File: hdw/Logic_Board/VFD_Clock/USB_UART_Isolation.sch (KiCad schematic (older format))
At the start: 12 parts

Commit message: Resurrected project
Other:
- moved on the sheet: C?, R?, U?

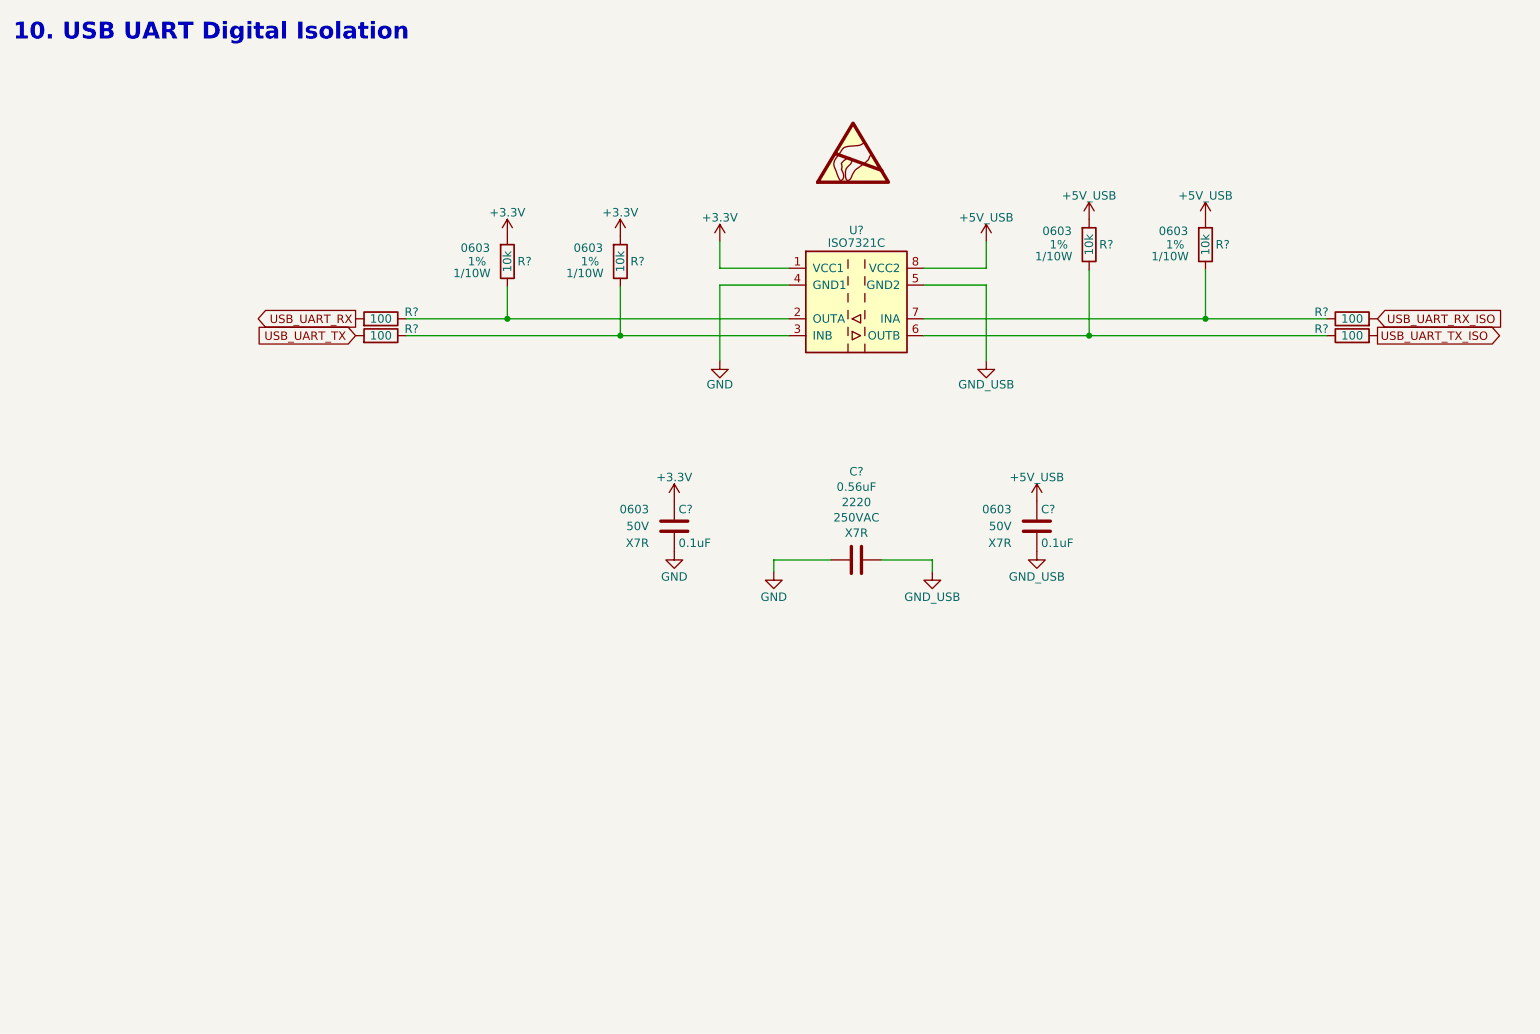
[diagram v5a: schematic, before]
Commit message: Added USB telemetry, isolation, and POS60_VAN current sense
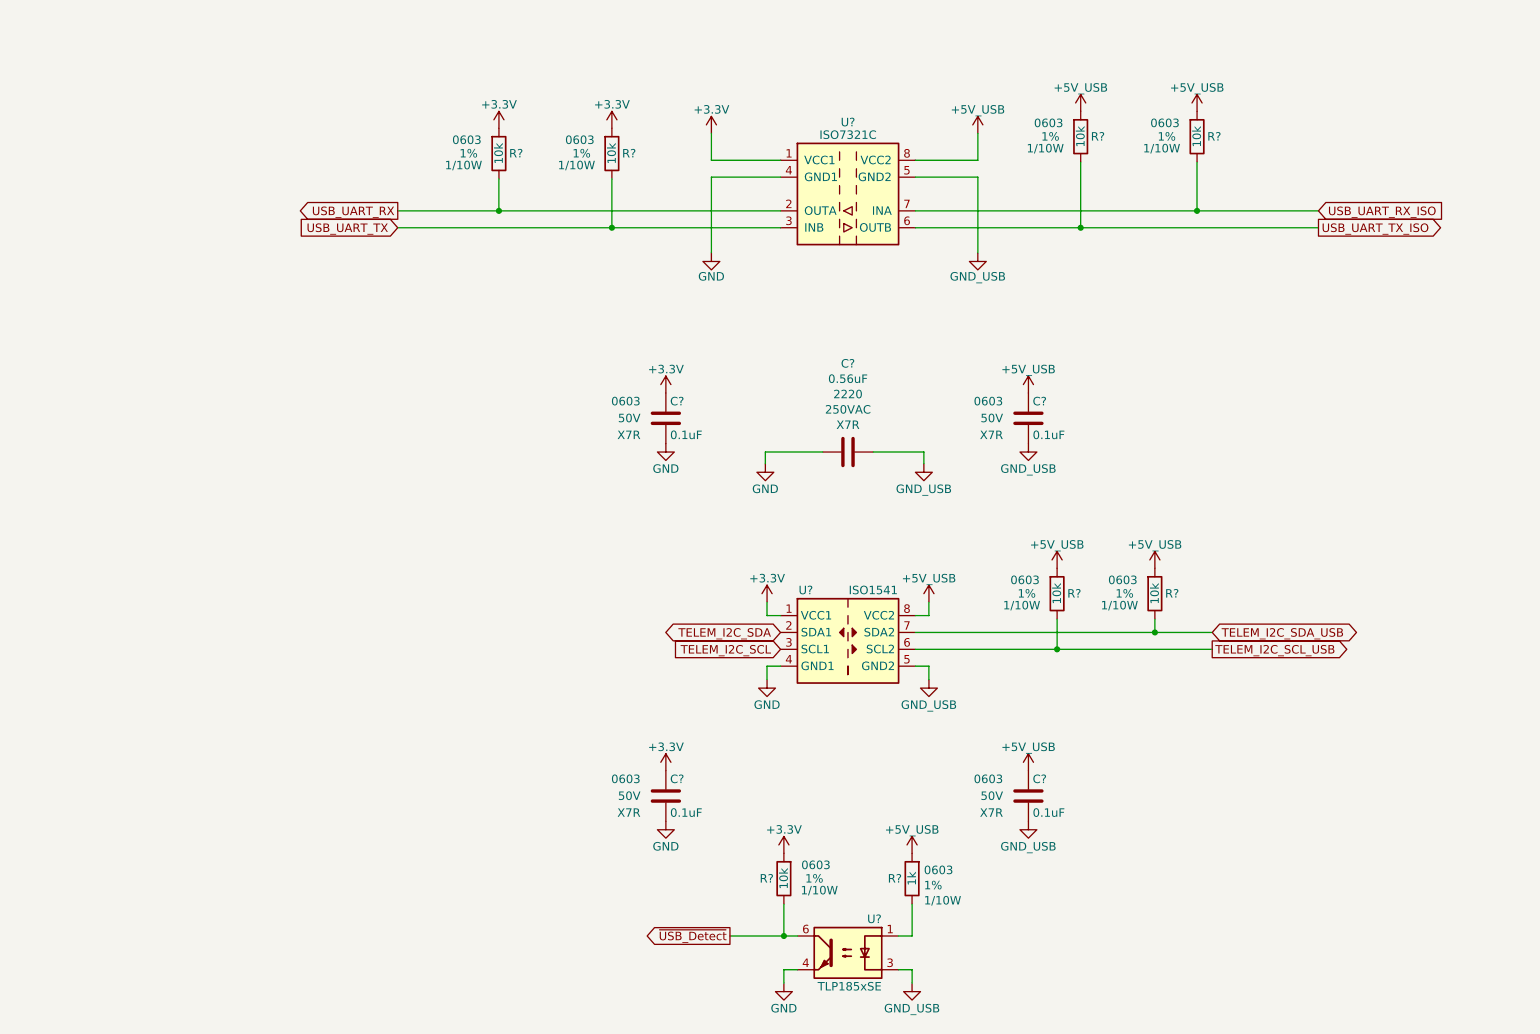
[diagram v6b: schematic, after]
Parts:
- removed R? (x4): 100, Resistors_SMD:R_0603, symbol Custom_Library:R_Custom
- added C? (x2): 0.1uF, Capacitors_SMD:C_0603, symbol Custom_Library:C_Custom
- added R? (x3): 10k, Resistors_SMD:R_0603, symbol Custom_Library:R_Custom
- added R?: 1k, symbol Custom_Library:R_Custom
- added U?: ISO1541, Package_SO:SOIC-8_3.9x4.9mm_P1.27mm, symbol Isolator:ISO1541
- added U?: TLP185xSE, Package_SO:SOIC-4_4.55x3.7mm_P2.54mm, symbol Isolator:TLP185xSE
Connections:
- net +3V3: now also C?.1, R?.1, U?.1 (VCC1)
- net +5V_USB: now also C?.1, R?.1, R?.1, R?.1, U?.8 (VCC2)
- net GND: now also C?.2, U?.4, U?.4 (GND1)
- net GND_USB: now also C?.2, U?.3, U?.5 (GND2)
- net USB_UART_RX: now also R?.2, U?.2 (OUTA)
- net USB_UART_RX_ISO: now also R?.2, U?.7 (INA)
- net USB_UART_TX: now also R?.2, U?.3 (INB)
- net USB_UART_TX_ISO: now also R?.2, U?.6 (OUTB)
- new net: R?.2, U?.1
- new net TELEM_I2C_SCL: U?.3 (SCL1)
- new net TELEM_I2C_SCL_USB: R?.2, U?.6 (SCL2)
- new net TELEM_I2C_SDA: U?.2 (SDA1)
- new net TELEM_I2C_SDA_USB: R?.2, U?.7 (SDA2)
- new net ~USB_Detect: R?.2, U?.6
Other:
- note removed: "10. USB UART Digital Isolation"
- moved on the sheet: C?, R?, U?

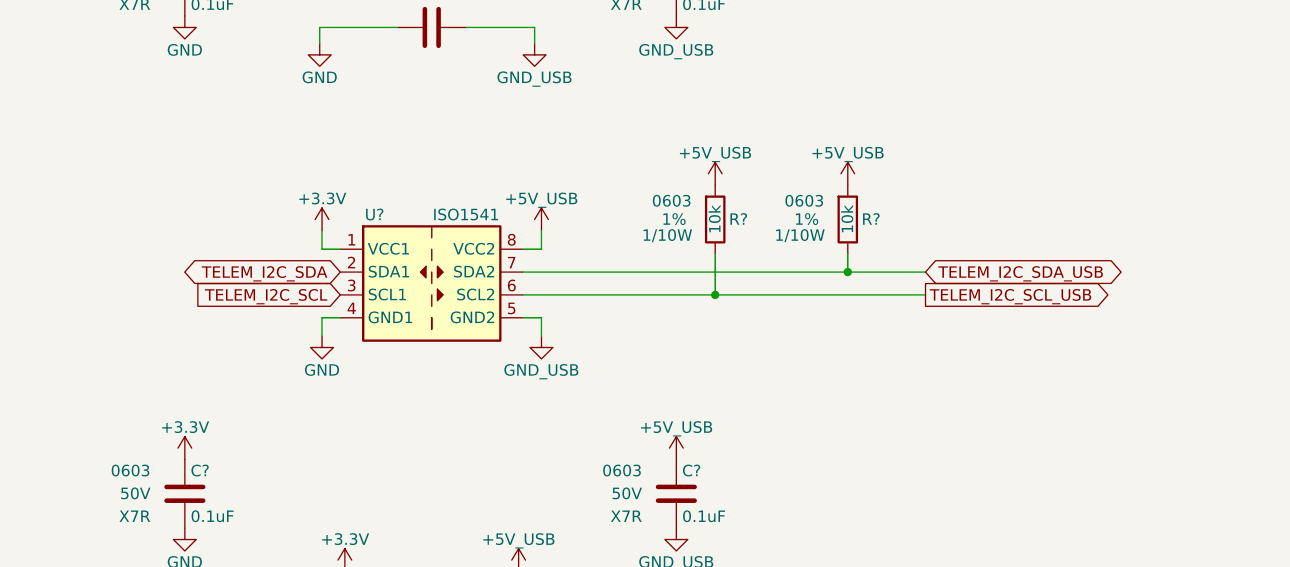
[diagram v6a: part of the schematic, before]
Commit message: Lots of schematic additions
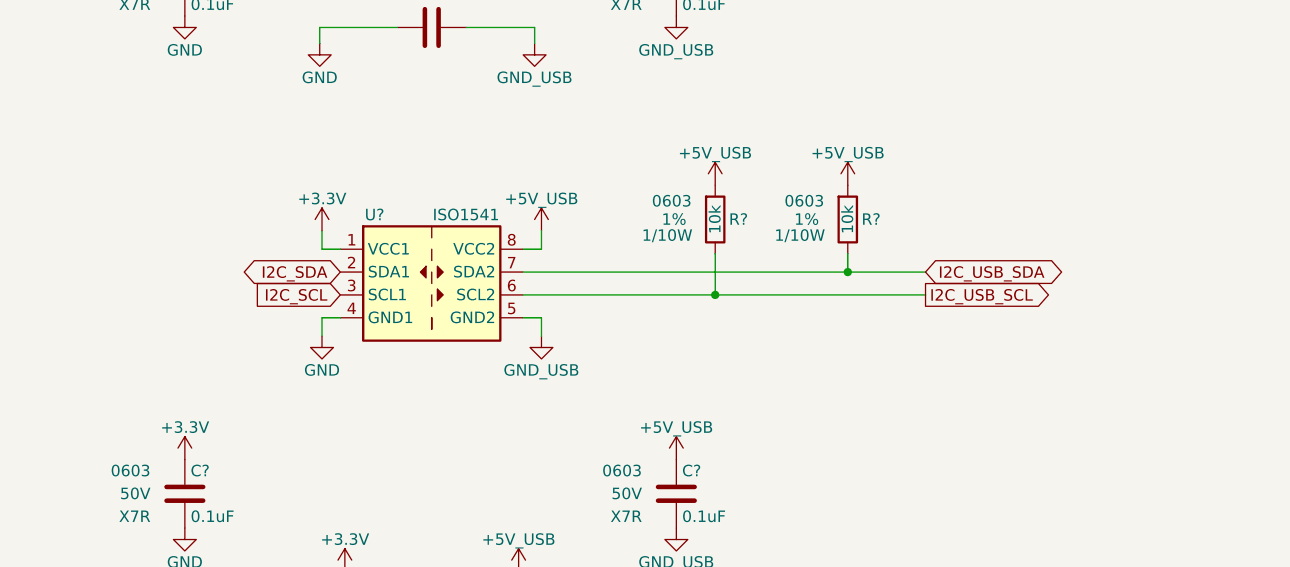
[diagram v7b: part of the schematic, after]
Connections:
- net TELEM_I2C_SCL renamed I2C_SCL
- net TELEM_I2C_SCL_USB renamed I2C_USB_SCL
- net TELEM_I2C_SDA renamed I2C_SDA
- net TELEM_I2C_SDA_USB renamed I2C_USB_SDA
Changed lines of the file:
@@
 $Descr A 11000 8500
 encoding utf-8
-Sheet 7 26
+Sheet 7 28
 Title "VFD Clock"
 Date "2019-04-11"
@@
 $EndComp
 Text GLabel 5100 4200 0    50   BiDi ~ 0
-TELEM_I2C_SDA
+I2C_SDA
 Text GLabel 5100 4300 0    50   Input ~ 0
-TELEM_I2C_SCL
+I2C_SCL
 Wire Wire Line
 	7660 4200 7320 4200
@@
 $EndComp
 Text GLabel 7660 4300 2    50   Output ~ 0
-TELEM_I2C_SCL_USB
+I2C_USB_SCL
 Text GLabel 7660 4200 2    50   BiDi ~ 0
-TELEM_I2C_SDA_USB
+I2C_USB_SDA
 $Comp
 L Custom_Library:C_Custom C?

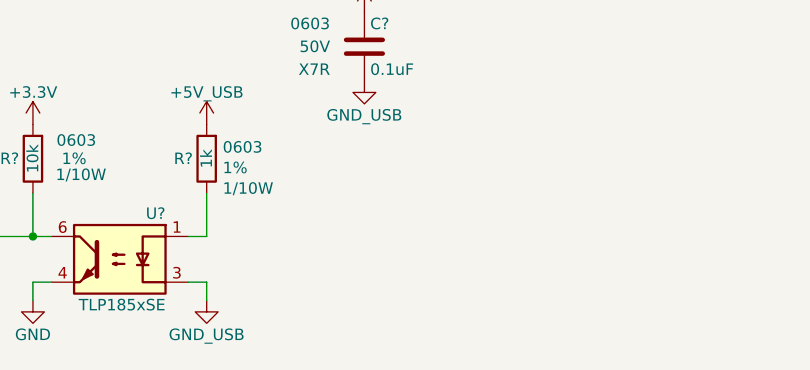
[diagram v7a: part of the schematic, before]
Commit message: Started IV-6 display board, continued logic board development
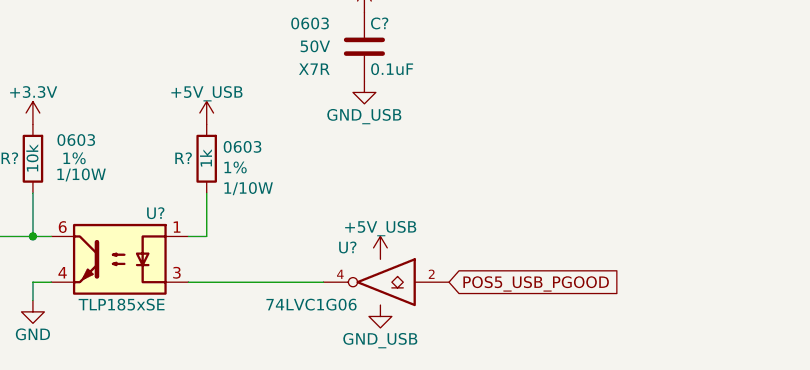
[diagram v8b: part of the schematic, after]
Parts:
- added U?: 74LVC1G06, TO_SOT_Packages_SMD:SOT-353_SC-70-5, symbol Custom_Library:74LVC1G06_Power
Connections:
- net +5V_USB: now also U?.5 (VCC)
- net GND_USB: now also U?.3 (GND); no longer U?.3
- new net: U?.3, U?.4
- new net POS5_USB_PGOOD: U?.2
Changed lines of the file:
@@
 	1    0    0    -1
 $EndComp
-$Comp
-L Custom_Library:GND_USB #PWR?
-U 1 1 5E0AFA5F
-P 5880 6280
-F 0 "#PWR?" H 5880 6030 50  0001 C CNN
-F 1 "GND_USB" H 5880 6130 50  0000 C CNN
-F 2 "" H 5880 6280 50  0001 C CNN
-F 3 "" H 5880 6280 50  0001 C CNN
-	1    5880 6280
-	1    0    0    -1
-$EndComp
-Wire Wire Line
-	5880 6280 5880 6200
-Wire Wire Line
-	5880 6200 5800 6200
 Wire Wire Line
 	5120 6280 5120 6200
@@
 Wire Wire Line
 	5120 6000 5120 5810
+Text GLabel 4800 6000 0    50   Output ~ 0
+~USB_Detect
+Wire Wire Line
+	4800 6000 5120 6000
+Connection ~ 5120 6000
+$Comp
+L Custom_Library:+5V_USB #PWR?
+U 1 1 5E0BA4BC
+P 5880 5510
+AR Path="/5BAAE1F3/5E0BA4BC" Ref="#PWR?"  Part="1"
+AR Path="/5BAAE1DC/5E0BA4BC" Ref="#PWR?"  Part="1"
+AR Path="/5CAD2DA3/5E0BA4BC" Ref="#PWR?"  Part="1"
+F 0 "#PWR?" H 5880 5360 50  0001 C CNN
+F 1 "+5V_USB" H 5880 5650 50  0000 C CNN
+F 2 "" H 5880 5510 50  0001 C CNN
+F 3 "" H 5880 5510 50  0001 C CNN
+	1    5880 5510
+	1    0    0    -1
+$EndComp
 $Comp
 L Custom_Library:R_Custom R?
@@
 $EndComp
 Wire Wire Line
+	5880 6000 5800 6000
+Wire Wire Line
 	5880 5810 5880 6000
+$Comp
+L Custom_Library:74LVC1G06_Power U?
+U 1 1 5E1C530D
+P 6640 6200
+F 0 "U?" H 6740 6350 50  0000 L CNN
+F 1 "74LVC1G06" H 6740 6100 50  0000 L CNN
+F 2 "TO_SOT_Packages_SMD:SOT-353_SC-70-5" H 6640 6250 50  0001 C CNN
+F 3 "http://www.ti.com/lit/ds/symlink/sn74lvc1g06.pdf" H 6640 6200 50  0001 C CNN
+F 4 "296-8484-1-ND" H 6640 6200 50  0001 C CNN "Digi-Key PN"
+	1    6640 6200
+	-1   0    0    -1
+$EndComp
 Wire Wire Line
-	5880 6000 5800 6000
+	6390 6200 5800 6200
 $Comp
 L Custom_Library:+5V_USB #PWR?
-U 1 1 5E0BA4BC
-P 5880 5510
-AR Path="/5BAAE1F3/5E0BA4BC" Ref="#PWR?"  Part="1"
-AR Path="/5BAAE1DC/5E0BA4BC" Ref="#PWR?"  Part="1"
-AR Path="/5CAD2DA3/5E0BA4BC" Ref="#PWR?"  Part="1"
-F 0 "#PWR?" H 5880 5360 50  0001 C CNN
-F 1 "+5V_USB" H 5880 5650 50  0000 C CNN
-F 2 "" H 5880 5510 50  0001 C CNN
-F 3 "" H 5880 5510 50  0001 C CNN
-	1    5880 5510
+U 1 1 5E1C71F0
+P 6640 6100
+AR Path="/5BAAE1F3/5E1C71F0" Ref="#PWR?"  Part="1"
+AR Path="/5BAAE1DC/5E1C71F0" Ref="#PWR?"  Part="1"
+AR Path="/5CAD2DA3/5E1C71F0" Ref="#PWR?"  Part="1"
+F 0 "#PWR?" H 6640 5950 50  0001 C CNN
+F 1 "+5V_USB" H 6640 6240 50  0000 C CNN
+F 2 "" H 6640 6100 50  0001 C CNN
+F 3 "" H 6640 6100 50  0001 C CNN
+	1    6640 6100
 	1    0    0    -1
 $EndComp
-Text GLabel 4800 6000 0    50   Output ~ 0
-~USB_Detect
-Wire Wire Line
-	4800 6000 5120 6000
-Connection ~ 5120 6000
+$Comp
+L Custom_Library:GND_USB #PWR?
+U 1 1 5E1C7C26
+P 6640 6300
+F 0 "#PWR?" H 6640 6050 50  0001 C CNN
+F 1 "GND_USB" H 6640 6150 50  0000 C CNN
+F 2 "" H 6640 6300 50  0001 C CNN
+F 3 "" H 6640 6300 50  0001 C CNN
+	1    6640 6300
+	1    0    0    -1
+$EndComp
+Text GLabel 6940 6200 2    50   Input ~ 0
+POS5_USB_PGOOD
 $EndSCHEMATC
